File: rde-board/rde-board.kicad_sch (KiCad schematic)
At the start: 19 parts, among them J1 RPI conn, J2 Mouse / Joy 1, J3 Joy 2, U1 ULN2003A, U2 ULN2003A

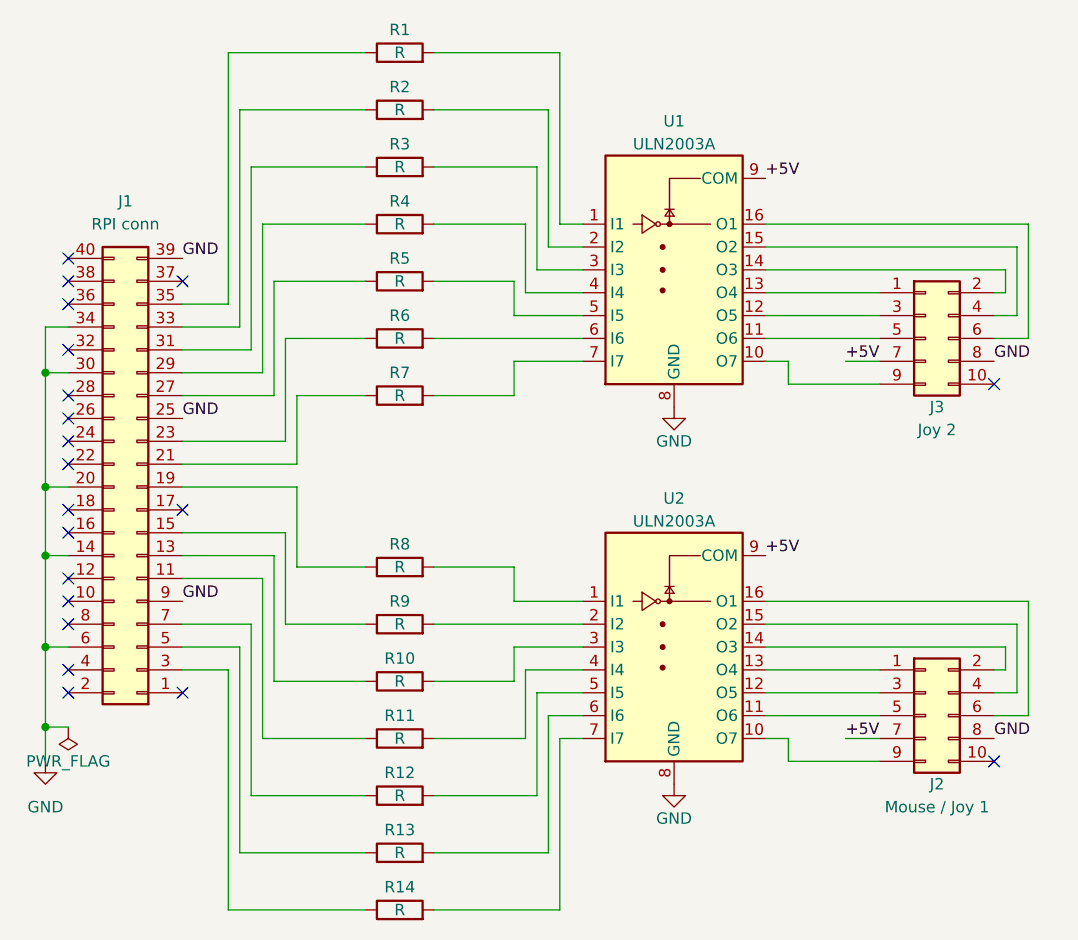
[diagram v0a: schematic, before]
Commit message: Fix ports connectors routing on board v2.1
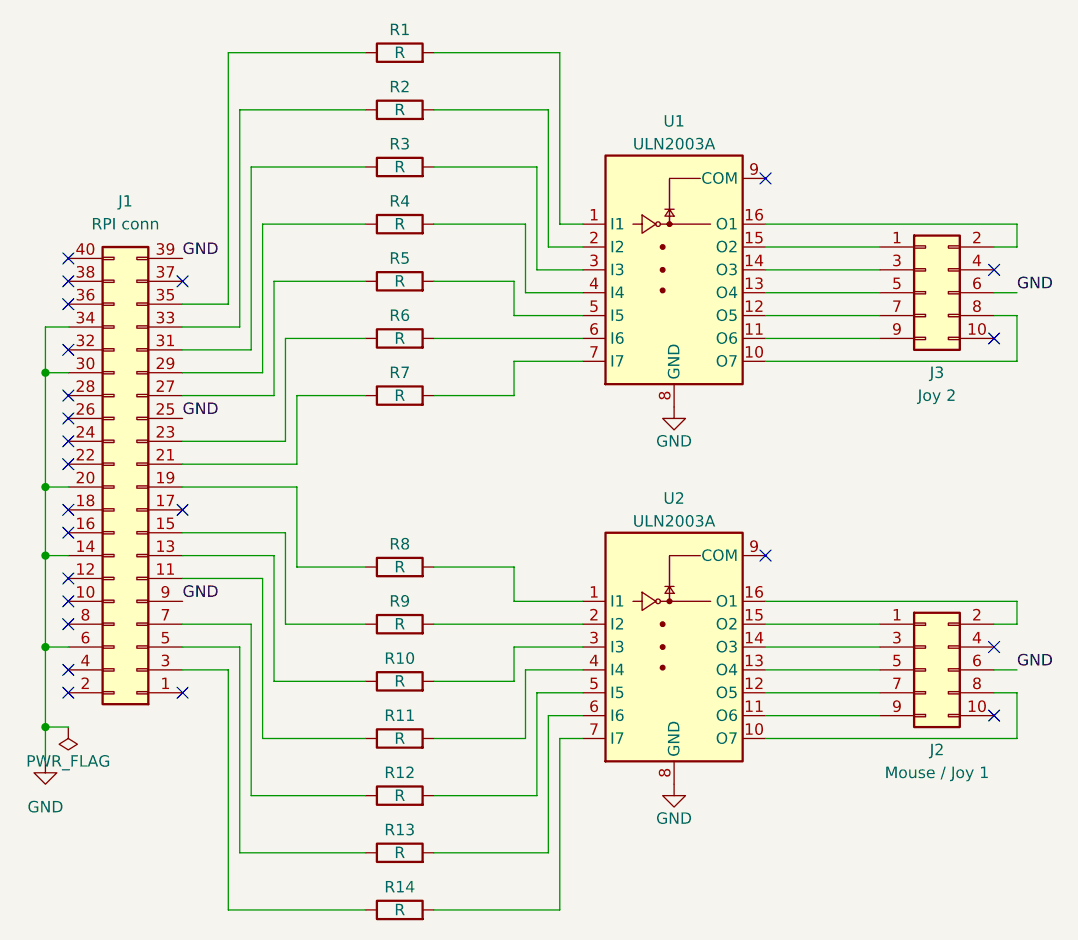
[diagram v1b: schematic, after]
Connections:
- net GND: now also J2.6 (Pin_6), J3.6 (Pin_6); no longer J2.8 (Pin_8), J3.8 (Pin_8)
- net at U2.10 (O7): now also J2.8 (Pin_8); no longer J2.9 (Pin_9)
- net at U2.11 (O6): now also J2.9 (Pin_9); no longer J2.5 (Pin_5)
- net at U2.12 (O5): now also J2.7 (Pin_7); no longer J2.3 (Pin_3)
- net at U2.13 (O4): now also J2.5 (Pin_5); no longer J2.1 (Pin_1)
- net at U2.14 (O3): now also J2.3 (Pin_3); no longer J2.2 (Pin_2)
- net at U2.15 (O2): now also J2.1 (Pin_1); no longer J2.4 (Pin_4)
- net at U2.16 (O1): now also J2.2 (Pin_2); no longer J2.6 (Pin_6)
- net at J3.1 (Pin_1): now also U1.15 (O2); no longer U1.13 (O4)
- net at J3.2 (Pin_2): now also U1.16 (O1); no longer U1.14 (O3)
- net at J3.3 (Pin_3): now also U1.14 (O3); no longer U1.12 (O5)
- net at J3.4 (Pin_4): no longer U1.15 (O2)
- net at J3.5 (Pin_5): now also U1.13 (O4); no longer U1.11 (O6)
- net at U1.10 (O7): now also J3.8 (Pin_8); no longer J3.9 (Pin_9)
- removed net +5V: J2.7 (Pin_7), J3.7 (Pin_7), U1.9 (COM), U2.9 (COM)
- new net: J3.7 (Pin_7), U1.12 (O5)
- new net: J3.9 (Pin_9), U1.11 (O6)
- no-connect marks 20 -> 24
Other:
- moved on the sheet: J2, J3
